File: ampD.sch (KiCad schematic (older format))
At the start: 8 parts, among them U4 MCP6004, U5 Mux

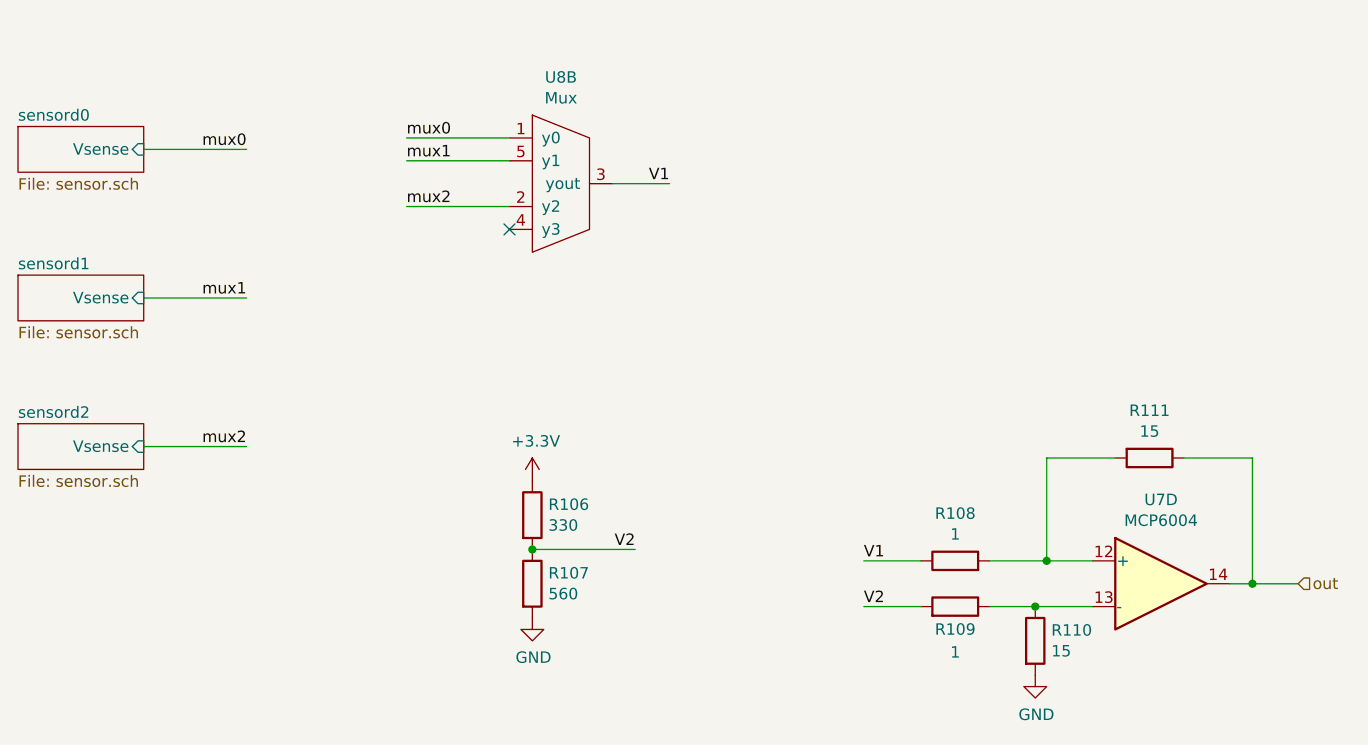
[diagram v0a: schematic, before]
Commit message: revised sensor connector
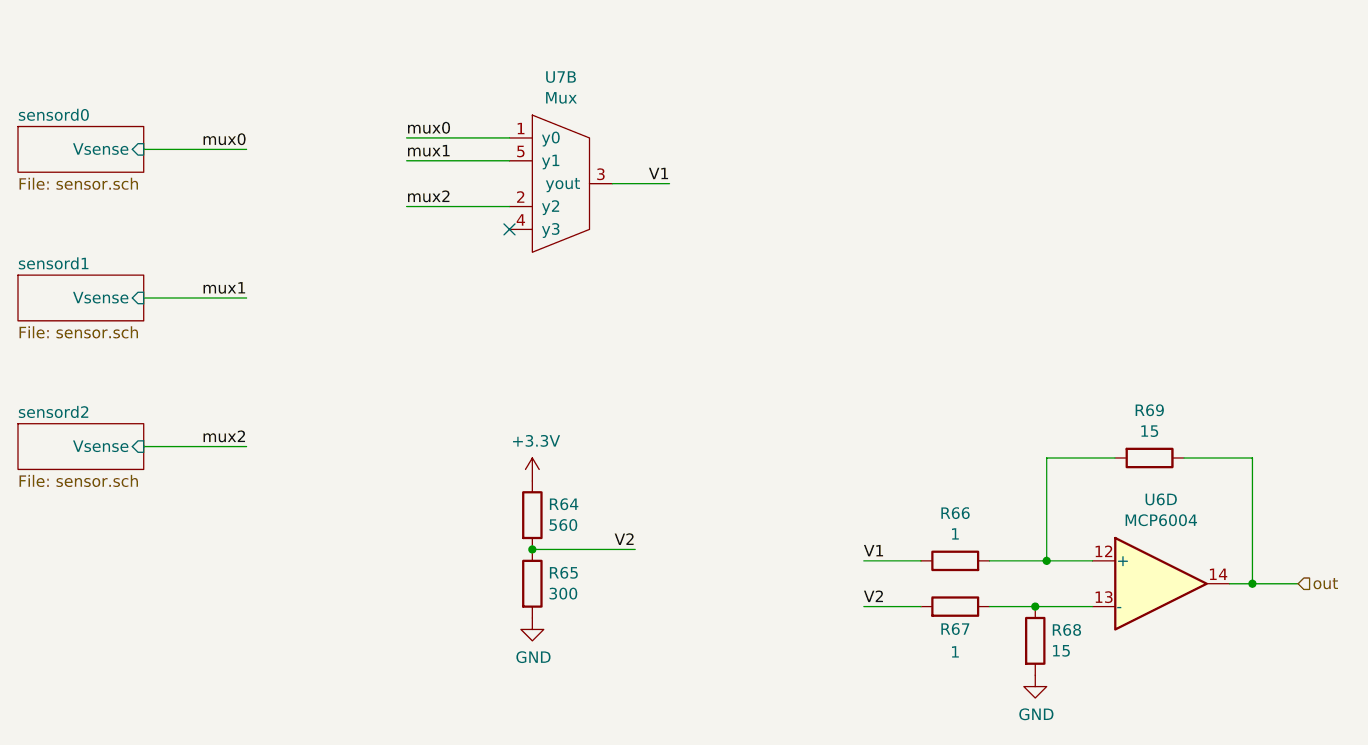
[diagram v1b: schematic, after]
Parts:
- R28: renamed from R46; value 330 -> 560
- R29: renamed from R47; value 560 -> 300
- renumbered R48 to R30, R49 to R31, R50 to R32, R51 to R33, U4 to U3, U5 to U4
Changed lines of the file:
@@
 $Descr A4 11693 8268
 encoding utf-8
-Sheet 27 41
+Sheet 30 41
 Title ""
 Date ""
@@
 AR Path="/6017DA21/6015EF5C" Ref="R?"  Part="1"
 AR Path="/601927EB/6015EF5C" Ref="R?"  Part="1"
-AR Path="/6019DBCE/6015EF5C" Ref="R50"  Part="1"
-AR Path="/601B4C19/6015EF5C" Ref="R110"  Part="1"
-F 0 "R110" H 5520 4096 50  0000 L CNN
+AR Path="/6019DBCE/6015EF5C" Ref="R32"  Part="1"
+AR Path="/601B4C19/6015EF5C" Ref="R68"  Part="1"
+F 0 "R68" H 5520 4096 50  0000 L CNN
 F 1 "15" H 5520 4005 50  0000 L CNN
 F 2 "Resistor_THT:R_Axial_DIN0204_L3.6mm_D1.6mm_P5.08mm_Horizontal" V 5380 4050 50  0001 C CNN
@@
 AR Path="/6017DA21/6019E3A7" Ref="R?"  Part="1"
 AR Path="/601927EB/6019E3A7" Ref="R?"  Part="1"
-AR Path="/6019DBCE/6019E3A7" Ref="R51"  Part="1"
-AR Path="/601B4C19/6019E3A7" Ref="R111"  Part="1"
-F 0 "R111" V 5743 3250 50  0000 C CNN
+AR Path="/6019DBCE/6019E3A7" Ref="R33"  Part="1"
+AR Path="/601B4C19/6019E3A7" Ref="R69"  Part="1"
+F 0 "R69" V 5743 3250 50  0000 C CNN
 F 1 "15" V 5834 3250 50  0000 C CNN
 F 2 "Resistor_THT:R_Axial_DIN0204_L3.6mm_D1.6mm_P5.08mm_Horizontal" V 5880 3250 50  0001 C CNN
@@
 AR Path="/6017DA21/6019E3B2" Ref="R?"  Part="1"
 AR Path="/601927EB/6019E3B2" Ref="R?"  Part="1"
-AR Path="/6019DBCE/6019E3B2" Ref="R48"  Part="1"
-AR Path="/601B4C19/6019E3B2" Ref="R108"  Part="1"
-F 0 "R108" V 5307 3700 50  0000 C CNN
+AR Path="/6019DBCE/6019E3B2" Ref="R30"  Part="1"
+AR Path="/601B4C19/6019E3B2" Ref="R66"  Part="1"
+F 0 "R66" V 5307 3700 50  0000 C CNN
 F 1 "1" V 5216 3700 50  0000 C CNN
 F 2 "Resistor_THT:R_Axial_DIN0204_L3.6mm_D1.6mm_P5.08mm_Horizontal" V 5030 3700 50  0001 C CNN
@@
 AR Path="/6017DA21/6019E3A8" Ref="R?"  Part="1"
 AR Path="/601927EB/6019E3A8" Ref="R?"  Part="1"
-AR Path="/6019DBCE/6019E3A8" Ref="R49"  Part="1"
-AR Path="/601B4C19/6019E3A8" Ref="R109"  Part="1"
-F 0 "R109" V 5000 3900 50  0000 C CNN
+AR Path="/6019DBCE/6019E3A8" Ref="R31"  Part="1"
+AR Path="/601B4C19/6019E3A8" Ref="R67"  Part="1"
+F 0 "R67" V 5000 3900 50  0000 C CNN
 F 1 "1" V 4900 3900 50  0000 C CNN
 F 2 "Resistor_THT:R_Axial_DIN0204_L3.6mm_D1.6mm_P5.08mm_Horizontal" V 5030 3900 50  0001 C CNN
@@
 AR Path="/6017DA21/6019E3B3" Ref="R?"  Part="1"
 AR Path="/601927EB/6019E3B3" Ref="R?"  Part="1"
-AR Path="/6019DBCE/6019E3B3" Ref="R46"  Part="1"
-AR Path="/601B4C19/6019E3B3" Ref="R106"  Part="1"
-F 0 "R106" H 3320 3546 50  0000 L CNN
-F 1 "330" H 3320 3455 50  0000 L CNN
+AR Path="/6019DBCE/6019E3B3" Ref="R28"  Part="1"
+AR Path="/601B4C19/6019E3B3" Ref="R64"  Part="1"
+F 0 "R64" H 3320 3546 50  0000 L CNN
+F 1 "560" H 3320 3455 50  0000 L CNN
 F 2 "Resistor_THT:R_Axial_DIN0204_L3.6mm_D1.6mm_P5.08mm_Horizontal" V 3180 3500 50  0001 C CNN
 F 3 "~" H 3250 3500 50  0001 C CNN
@@
 AR Path="/6017DA21/60198F36" Ref="R?"  Part="1"
 AR Path="/601927EB/60198F36" Ref="R?"  Part="1"
-AR Path="/6019DBCE/60198F36" Ref="R47"  Part="1"
-AR Path="/601B4C19/60198F36" Ref="R107"  Part="1"
-F 0 "R107" H 3320 3846 50  0000 L CNN
-F 1 "560" H 3320 3755 50  0000 L CNN
+AR Path="/6019DBCE/60198F36" Ref="R29"  Part="1"
+AR Path="/601B4C19/60198F36" Ref="R65"  Part="1"
+F 0 "R65" H 3320 3846 50  0000 L CNN
+F 1 "300" H 3320 3755 50  0000 L CNN
 F 2 "Resistor_THT:R_Axial_DIN0204_L3.6mm_D1.6mm_P5.08mm_Horizontal" V 3180 3800 50  0001 C CNN
 F 3 "~" H 3250 3800 50  0001 C CNN
@@
 AR Path="/6017DA21/60198F37" Ref="#PWR?"  Part="1"
 AR Path="/601927EB/60198F37" Ref="#PWR?"  Part="1"
-AR Path="/6019DBCE/60198F37" Ref="#PWR077"  Part="1"
-AR Path="/601B4C19/60198F37" Ref="#PWR0167"  Part="1"
-F 0 "#PWR0167" H 3250 3200 50  0001 C CNN
+AR Path="/6019DBCE/60198F37" Ref="#PWR041"  Part="1"
+AR Path="/601B4C19/60198F37" Ref="#PWR083"  Part="1"
+F 0 "#PWR083" H 3250 3200 50  0001 C CNN
 F 1 "+3.3V" H 3265 3523 50  0000 C CNN
 F 2 "" H 3250 3350 50  0001 C CNN
@@
 AR Path="/6017DA21/6019E3A9" Ref="#PWR?"  Part="1"
 AR Path="/601927EB/6019E3A9" Ref="#PWR?"  Part="1"
-AR Path="/6019DBCE/6019E3A9" Ref="#PWR078"  Part="1"
-AR Path="/601B4C19/6019E3A9" Ref="#PWR0168"  Part="1"
-F 0 "#PWR0168" H 3250 3700 50  0001 C CNN
+AR Path="/6019DBCE/6019E3A9" Ref="#PWR042"  Part="1"
+AR Path="/601B4C19/6019E3A9" Ref="#PWR084"  Part="1"
+F 0 "#PWR084" H 3250 3700 50  0001 C CNN
 F 1 "GND" H 3255 3777 50  0000 C CNN
 F 2 "" H 3250 3950 50  0001 C CNN
@@
 AR Path="/6017DA21/60198F29" Ref="#PWR?"  Part="1"
 AR Path="/601927EB/60198F29" Ref="#PWR?"  Part="1"
-AR Path="/6019DBCE/60198F29" Ref="#PWR079"  Part="1"
-AR Path="/601B4C19/60198F29" Ref="#PWR0169"  Part="1"
-F 0 "#PWR0169" H 5450 3950 50  0001 C CNN
+AR Path="/6019DBCE/60198F29" Ref="#PWR043"  Part="1"
+AR Path="/601B4C19/60198F29" Ref="#PWR085"  Part="1"
+F 0 "#PWR085" H 5450 3950 50  0001 C CNN
 F 1 "GND" H 5455 4027 50  0000 C CNN
 F 2 "" H 5450 4200 50  0001 C CNN
@@
 mux2
 $Comp
-L PNG_PCB_Parts:Mux U5
+L PNG_PCB_Parts:Mux U4
 U 2 1 6017A5CD
 P 3350 2050
-AR Path="/6019DBCE/6017A5CD" Ref="U5"  Part="2"
-AR Path="/601B4C19/6017A5CD" Ref="U8"  Part="2"
-F 0 "U8" H 3375 2515 50  0000 C CNN
+AR Path="/6019DBCE/6017A5CD" Ref="U4"  Part="2"
+AR Path="/601B4C19/6017A5CD" Ref="U7"  Part="2"
+F 0 "U7" H 3375 2515 50  0000 C CNN
 F 1 "Mux" H 3375 2424 50  0000 C CNN
 F 2 "Package_DIP:DIP-16_W7.62mm" H 3350 2050 50  0001 C CNN
@@
 $EndComp
 $Comp
-L Amplifier_Operational:MCP6004 U4
+L Amplifier_Operational:MCP6004 U3
 U 4 1 6018F24E
 P 6000 3800
-AR Path="/6019DBCE/6018F24E" Ref="U4"  Part="4"
-AR Path="/601B4C19/6018F24E" Ref="U7"  Part="4"
-F 0 "U7" H 6000 4167 50  0000 C CNN
+AR Path="/6019DBCE/6018F24E" Ref="U3"  Part="4"
+AR Path="/601B4C19/6018F24E" Ref="U6"  Part="4"
+F 0 "U6" H 6000 4167 50  0000 C CNN
 F 1 "MCP6004" H 6000 4076 50  0000 C CNN
 F 2 "Package_DIP:DIP-14_W7.62mm" H 5950 3900 50  0001 C CNN

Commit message: moved sensor r div to other side of mux
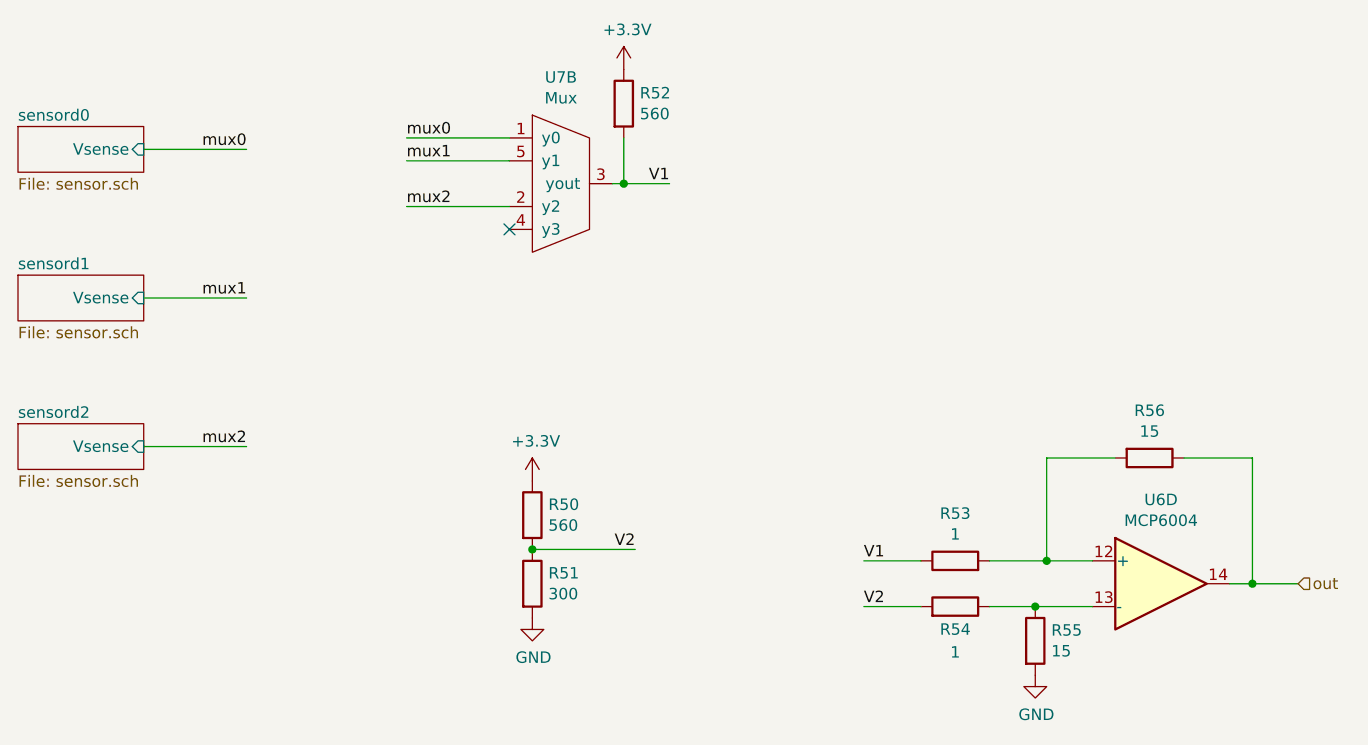
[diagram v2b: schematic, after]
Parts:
- added R24: 560, Resistor_THT:R_Axial_DIN0204_L3.6mm_D1.6mm_P5.08mm_Horizontal, symbol Device:R
- renumbered R28 to R22, R29 to R23, R30 to R25, R31 to R26, R32 to R27, R33 to R28
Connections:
- net +3V3: now also R24.1
- net V1: now also R24.2
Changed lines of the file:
@@
 $Descr A4 11693 8268
 encoding utf-8
-Sheet 30 41
+Sheet 14 41
 Title ""
 Date ""
@@
 AR Path="/6017DA21/6015EF5C" Ref="R?"  Part="1"
 AR Path="/601927EB/6015EF5C" Ref="R?"  Part="1"
-AR Path="/6019DBCE/6015EF5C" Ref="R32"  Part="1"
-AR Path="/601B4C19/6015EF5C" Ref="R68"  Part="1"
-F 0 "R68" H 5520 4096 50  0000 L CNN
+AR Path="/6019DBCE/6015EF5C" Ref="R27"  Part="1"
+AR Path="/601B4C19/6015EF5C" Ref="R55"  Part="1"
+F 0 "R55" H 5520 4096 50  0000 L CNN
 F 1 "15" H 5520 4005 50  0000 L CNN
 F 2 "Resistor_THT:R_Axial_DIN0204_L3.6mm_D1.6mm_P5.08mm_Horizontal" V 5380 4050 50  0001 C CNN
@@
 AR Path="/6017DA21/6019E3A7" Ref="R?"  Part="1"
 AR Path="/601927EB/6019E3A7" Ref="R?"  Part="1"
-AR Path="/6019DBCE/6019E3A7" Ref="R33"  Part="1"
-AR Path="/601B4C19/6019E3A7" Ref="R69"  Part="1"
-F 0 "R69" V 5743 3250 50  0000 C CNN
+AR Path="/6019DBCE/6019E3A7" Ref="R28"  Part="1"
+AR Path="/601B4C19/6019E3A7" Ref="R56"  Part="1"
+F 0 "R56" V 5743 3250 50  0000 C CNN
 F 1 "15" V 5834 3250 50  0000 C CNN
 F 2 "Resistor_THT:R_Axial_DIN0204_L3.6mm_D1.6mm_P5.08mm_Horizontal" V 5880 3250 50  0001 C CNN
@@
 AR Path="/6017DA21/6019E3B2" Ref="R?"  Part="1"
 AR Path="/601927EB/6019E3B2" Ref="R?"  Part="1"
-AR Path="/6019DBCE/6019E3B2" Ref="R30"  Part="1"
-AR Path="/601B4C19/6019E3B2" Ref="R66"  Part="1"
-F 0 "R66" V 5307 3700 50  0000 C CNN
+AR Path="/6019DBCE/6019E3B2" Ref="R25"  Part="1"
+AR Path="/601B4C19/6019E3B2" Ref="R53"  Part="1"
+F 0 "R53" V 5307 3700 50  0000 C CNN
 F 1 "1" V 5216 3700 50  0000 C CNN
 F 2 "Resistor_THT:R_Axial_DIN0204_L3.6mm_D1.6mm_P5.08mm_Horizontal" V 5030 3700 50  0001 C CNN
@@
 AR Path="/6017DA21/6019E3A8" Ref="R?"  Part="1"
 AR Path="/601927EB/6019E3A8" Ref="R?"  Part="1"
-AR Path="/6019DBCE/6019E3A8" Ref="R31"  Part="1"
-AR Path="/601B4C19/6019E3A8" Ref="R67"  Part="1"
-F 0 "R67" V 5000 3900 50  0000 C CNN
+AR Path="/6019DBCE/6019E3A8" Ref="R26"  Part="1"
+AR Path="/601B4C19/6019E3A8" Ref="R54"  Part="1"
+F 0 "R54" V 5000 3900 50  0000 C CNN
 F 1 "1" V 4900 3900 50  0000 C CNN
 F 2 "Resistor_THT:R_Axial_DIN0204_L3.6mm_D1.6mm_P5.08mm_Horizontal" V 5030 3900 50  0001 C CNN
@@
 	4950 3900 4700 3900
 Wire Wire Line
-	3600 2050 3850 2050
+	3600 2050 3650 2050
 Text Label 3850 2050 2    50   ~ 0
 V1
@@
 AR Path="/6017DA21/6019E3B3" Ref="R?"  Part="1"
 AR Path="/601927EB/6019E3B3" Ref="R?"  Part="1"
-AR Path="/6019DBCE/6019E3B3" Ref="R28"  Part="1"
-AR Path="/601B4C19/6019E3B3" Ref="R64"  Part="1"
-F 0 "R64" H 3320 3546 50  0000 L CNN
+AR Path="/6019DBCE/6019E3B3" Ref="R22"  Part="1"
+AR Path="/601B4C19/6019E3B3" Ref="R50"  Part="1"
+F 0 "R50" H 3320 3546 50  0000 L CNN
 F 1 "560" H 3320 3455 50  0000 L CNN
 F 2 "Resistor_THT:R_Axial_DIN0204_L3.6mm_D1.6mm_P5.08mm_Horizontal" V 3180 3500 50  0001 C CNN
@@
 AR Path="/6017DA21/60198F36" Ref="R?"  Part="1"
 AR Path="/601927EB/60198F36" Ref="R?"  Part="1"
-AR Path="/6019DBCE/60198F36" Ref="R29"  Part="1"
-AR Path="/601B4C19/60198F36" Ref="R65"  Part="1"
-F 0 "R65" H 3320 3846 50  0000 L CNN
+AR Path="/6019DBCE/60198F36" Ref="R23"  Part="1"
+AR Path="/601B4C19/60198F36" Ref="R51"  Part="1"
+F 0 "R51" H 3320 3846 50  0000 L CNN
 F 1 "300" H 3320 3755 50  0000 L CNN
 F 2 "Resistor_THT:R_Axial_DIN0204_L3.6mm_D1.6mm_P5.08mm_Horizontal" V 3180 3800 50  0001 C CNN
@@
 AR Path="/6017DA21/60198F37" Ref="#PWR?"  Part="1"
 AR Path="/601927EB/60198F37" Ref="#PWR?"  Part="1"
-AR Path="/6019DBCE/60198F37" Ref="#PWR041"  Part="1"
-AR Path="/601B4C19/60198F37" Ref="#PWR083"  Part="1"
-F 0 "#PWR083" H 3250 3200 50  0001 C CNN
+AR Path="/6019DBCE/60198F37" Ref="#PWR035"  Part="1"
+AR Path="/601B4C19/60198F37" Ref="#PWR069"  Part="1"
+F 0 "#PWR069" H 3250 3200 50  0001 C CNN
 F 1 "+3.3V" H 3265 3523 50  0000 C CNN
 F 2 "" H 3250 3350 50  0001 C CNN
@@
 AR Path="/6017DA21/6019E3A9" Ref="#PWR?"  Part="1"
 AR Path="/601927EB/6019E3A9" Ref="#PWR?"  Part="1"
-AR Path="/6019DBCE/6019E3A9" Ref="#PWR042"  Part="1"
-AR Path="/601B4C19/6019E3A9" Ref="#PWR084"  Part="1"
-F 0 "#PWR084" H 3250 3700 50  0001 C CNN
+AR Path="/6019DBCE/6019E3A9" Ref="#PWR036"  Part="1"
+AR Path="/601B4C19/6019E3A9" Ref="#PWR070"  Part="1"
+F 0 "#PWR070" H 3250 3700 50  0001 C CNN
 F 1 "GND" H 3255 3777 50  0000 C CNN
 F 2 "" H 3250 3950 50  0001 C CNN
@@
 AR Path="/6017DA21/60198F29" Ref="#PWR?"  Part="1"
 AR Path="/601927EB/60198F29" Ref="#PWR?"  Part="1"
-AR Path="/6019DBCE/60198F29" Ref="#PWR043"  Part="1"
-AR Path="/601B4C19/60198F29" Ref="#PWR085"  Part="1"
-F 0 "#PWR085" H 5450 3950 50  0001 C CNN
+AR Path="/6019DBCE/60198F29" Ref="#PWR038"  Part="1"
+AR Path="/601B4C19/60198F29" Ref="#PWR072"  Part="1"
+F 0 "#PWR072" H 5450 3950 50  0001 C CNN
 F 1 "GND" H 5455 4027 50  0000 C CNN
 F 2 "" H 5450 4200 50  0001 C CNN
@@
 F2 "Vsense" I R 1550 3200 50
 $EndSheet
+$Comp
+L Device:R R?
+U 1 1 60204E98
+P 3650 1700
+AR Path="/60132BC3/6013AE22/60204E98" Ref="R?"  Part="1"
+AR Path="/6017CC5E/60204E98" Ref="R?"  Part="1"
+AR Path="/6017DA21/60204E98" Ref="R?"  Part="1"
+AR Path="/601927EB/60204E98" Ref="R?"  Part="1"
+AR Path="/6019DBCE/60204E98" Ref="R24"  Part="1"
+AR Path="/601B4C19/60204E98" Ref="R52"  Part="1"
+F 0 "R52" H 3720 1746 50  0000 L CNN
+F 1 "560" H 3720 1655 50  0000 L CNN
+F 2 "Resistor_THT:R_Axial_DIN0204_L3.6mm_D1.6mm_P5.08mm_Horizontal" V 3580 1700 50  0001 C CNN
+F 3 "~" H 3650 1700 50  0001 C CNN
+	1    3650 1700
+	1    0    0    -1
+$EndComp
+$Comp
+L power:+3.3V #PWR?
+U 1 1 60204FC0
+P 3650 1550
+AR Path="/60132BC3/6013AE22/60204FC0" Ref="#PWR?"  Part="1"
+AR Path="/6017CC5E/60204FC0" Ref="#PWR?"  Part="1"
+AR Path="/6017DA21/60204FC0" Ref="#PWR?"  Part="1"
+AR Path="/601927EB/60204FC0" Ref="#PWR?"  Part="1"
+AR Path="/6019DBCE/60204FC0" Ref="#PWR037"  Part="1"
+AR Path="/601B4C19/60204FC0" Ref="#PWR071"  Part="1"
+F 0 "#PWR071" H 3650 1400 50  0001 C CNN
+F 1 "+3.3V" H 3665 1723 50  0000 C CNN
+F 2 "" H 3650 1550 50  0001 C CNN
+F 3 "" H 3650 1550 50  0001 C CNN
+	1    3650 1550
+	1    0    0    -1
+$EndComp
+Wire Wire Line
+	3650 1850 3650 2050
+Connection ~ 3650 2050
+Wire Wire Line
+	3650 2050 3850 2050
 $EndSCHEMATC
